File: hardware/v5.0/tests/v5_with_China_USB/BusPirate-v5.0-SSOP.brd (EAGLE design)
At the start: 50 x 50 mm, 49 parts, among them CON1 CON_HEADER_1X10-RIGHT_ANGLED_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, CON2 CON_HEADER_1X05-PTH, CON3 CON-USB-F-MICRO-B, IC1 PIC24FJ64GA002, IC2 4066, IC4 IC_FT230X-SSOP-16, IC5 IC_BL1551, IC6 IC_BL1551

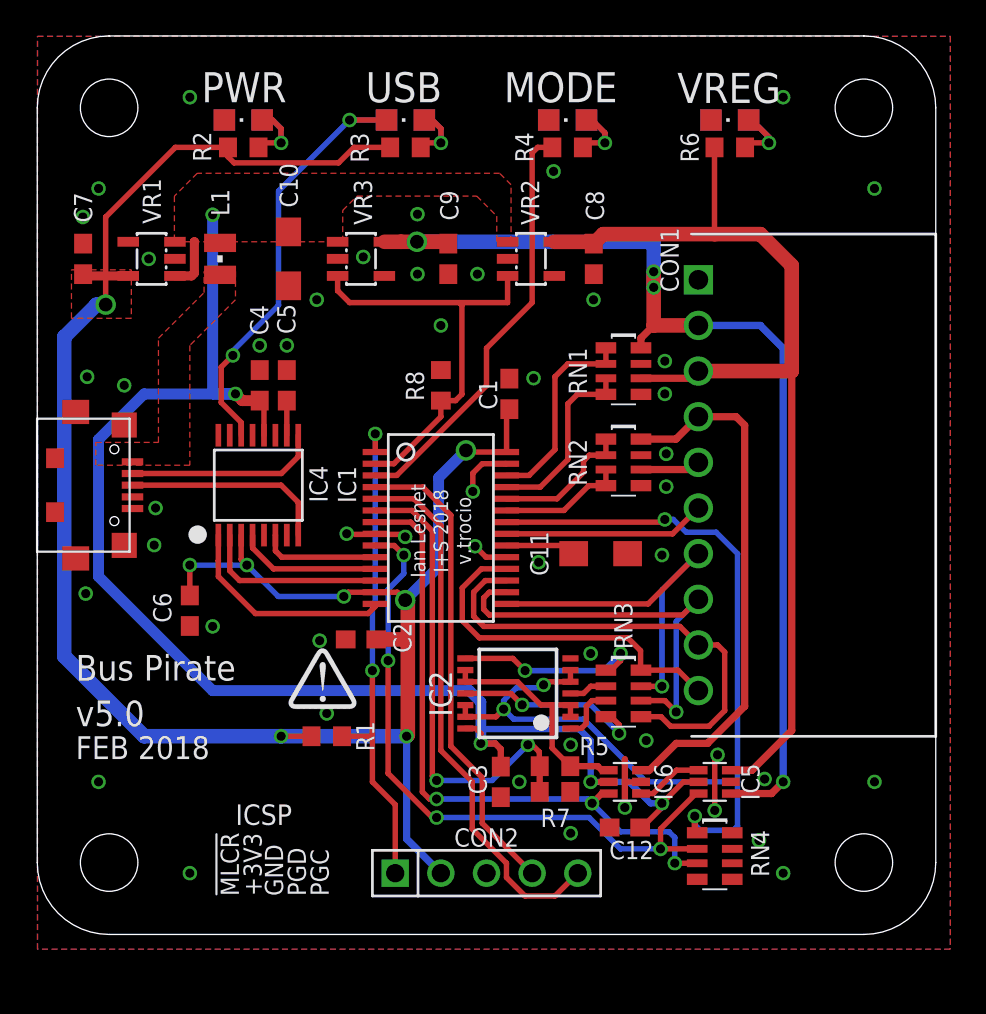
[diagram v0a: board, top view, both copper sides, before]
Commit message: Added v5 hardware with different USB Micro B style connectors
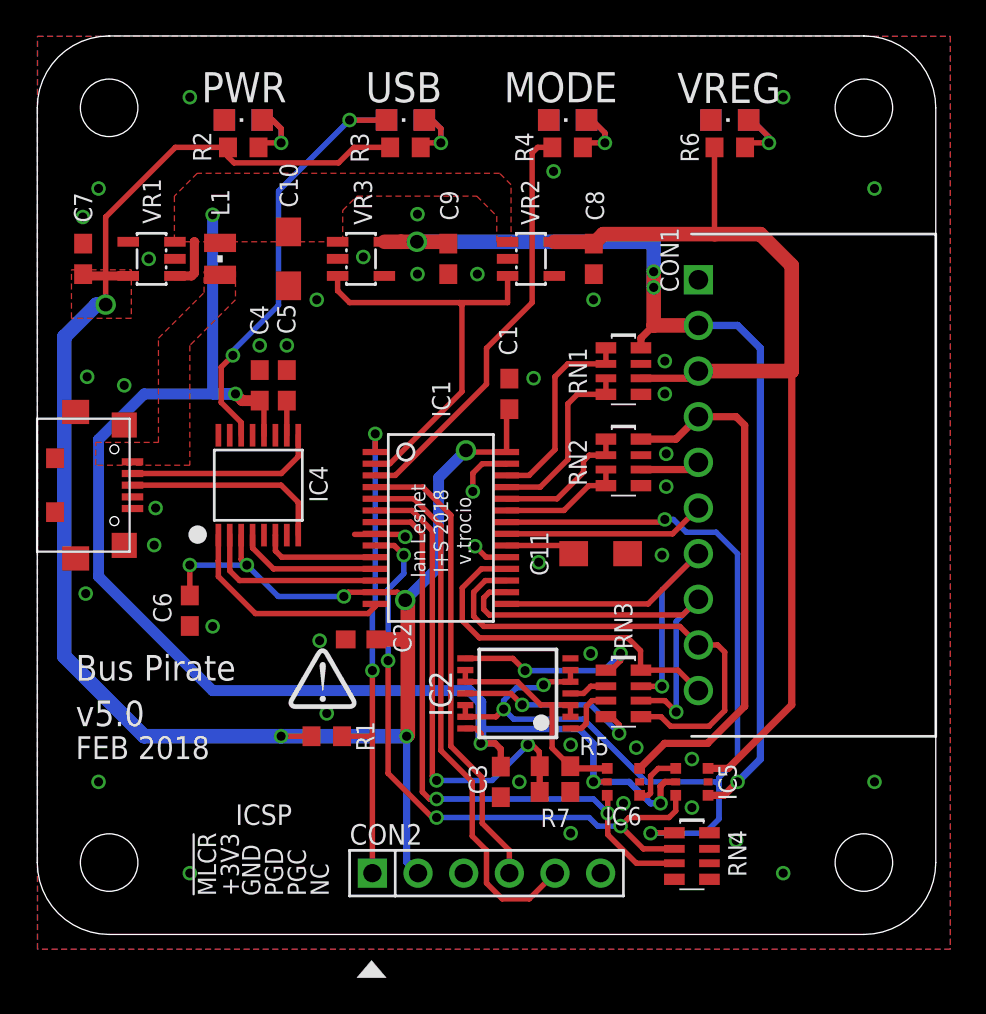
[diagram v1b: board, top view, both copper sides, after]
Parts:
- removed C12: 0.1uF, dp_devices:C603
- removed R8: 10K, dp_devices:R603
- CON2: value CON_HEADER_1X05-PTH -> CON_HEADER_1X06-PTH; device dp_devices.v6:M1X5 -> dp_devices.v6:M1X6
- IC5, IC6: device dp_devices.v6:SC-70-6 -> dp_devices.v6:SOT-363
- moved CON2 6.35 mm to (19.1, 3.81)
- moved IC5 1.27 mm to (36.8, 8.89)
- moved RN4 1.27 mm to (36.8, 4.76)
- moved IC6 0.08 mm to (33.0, 8.89)
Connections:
- net GND: no longer C12.2, R8.1
- net VREGEN: no longer R8.2
- net VUSB: no longer C12.1
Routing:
- net GND: track 14.5 -> 8.04 mm, vias 49 -> 46
- net VUSB: track 84.6 -> 81.4 mm
- net SWV50: track 59.1 -> 57.1 mm
- net V33PU: track 36.2 -> 34.6 mm, vias 3 -> 2
- net V50PU: track 37.3 -> 36.3 mm
- net VREGEN: track 24.1 -> 23.5 mm
- net N$12: track 3.74 -> 3.19 mm
- net +3V3: track 119.5 -> 119.0 mm
- net PGD: track 26.7 -> 26.1 mm
- net MCLR: track 27.7 -> 27.2 mm
